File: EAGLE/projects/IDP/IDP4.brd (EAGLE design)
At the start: 100 x 80 mm, 14 parts, among them IC1 LM348P, M1 IDP_PROTOBOARD, U1 LM393P

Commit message: Added LED :+1:
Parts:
- added LED1, LED2, LED3: LED_23MM, IDP_library:LED3MM
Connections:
- new net ERROR_SENSOR_MALF: LED2.A, M1.D2
- new net ERROR_SIGNAL: LED3.A, M1.D0
- net GND: now also LED2.K, LED3.K
- net PHOTO_ON: now also LED1.A, LED1.K
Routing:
- net ERROR_SIGNAL: track 0.00 -> 20.3 mm, vias 0 -> 2
- net ERROR_SENSOR_MALF: track 0.00 -> 12.7 mm, vias 0 -> 2
- net GND: track 76.4 -> 86.5 mm
- net PHOTO_ON: track 45.6 -> 43.0 mm
- net +5V: track 53.3 -> 52.2 mm
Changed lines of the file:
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@@
 <attribute name="MF" value="MOLEX" x="60.96" y="55.88" size="1.778" layer="27" rot="R180" display="off"/>
 <attribute name="MPN" value="" x="60.96" y="55.88" size="1.778" layer="27" rot="R180" display="off"/>
-<attribute name="NAME" x="58.4469" y="51.5351" size="1.016" layer="25" ratio="10"/>
+<attribute name="NAME" x="54.6369" y="52.8051" size="1.016" layer="25" ratio="10"/>
 <attribute name="OC_FARNELL" value="unknown" x="60.96" y="55.88" size="1.778" layer="27" rot="R180" display="off"/>
 <attribute name="OC_NEWARK" value="unknown" x="60.96" y="55.88" size="1.778" layer="27" rot="R180" display="off"/>
 <attribute name="POPULARITY" value="0" x="60.96" y="55.88" size="1.778" layer="27" rot="R180" display="off"/>
-<attribute name="VALUE" x="71.0931" y="50.3189" size="0.8128" layer="27" ratio="10" rot="R180"/>
+<attribute name="VALUE" x="66.0131" y="51.5889" size="0.8128" layer="27" ratio="10" rot="R180"/>
 </element>
 <element name="SERVO" library="IDP_library" package="7395-03" package3d_urn="urn:adsk.eagle:package:8078646/1" value="Rapid 22-1010 /  22-0910" x="52.07" y="55.88" smashed="yes" rot="R180">
@@
 <attribute name="SPICEPREFIX" value="R" x="34.29" y="46.99" size="1.778" layer="27" rot="R270" display="off"/>
 <attribute name="VALUE" x="31.9786" y="49.1236" size="1.27" layer="27" ratio="10" rot="R270"/>
+</element>
+<element name="LED1" library="IDP_library" package="LED3MM" package3d_urn="urn:adsk.eagle:package:15797/1" value="LED_23MM" x="72.39" y="52.07" smashed="yes" rot="R90">
+<attribute name="NAME" x="75.819" y="50.165" size="1.27" layer="25" ratio="10" rot="R90"/>
+<attribute name="POPULARITY" value="97" x="72.39" y="52.07" size="1.778" layer="27" rot="R90" display="off"/>
+</element>
+<element name="LED2" library="IDP_library" package="LED3MM" package3d_urn="urn:adsk.eagle:package:15797/1" value="LED_23MM" x="67.31" y="49.53" smashed="yes" rot="R270">
+<attribute name="NAME" x="60.325" y="47.371" size="1.27" layer="25" ratio="10"/>
+<attribute name="POPULARITY" value="97" x="67.31" y="49.53" size="1.778" layer="27" rot="R270" display="off"/>
+</element>
+<element name="LED3" library="IDP_library" package="LED3MM" package3d_urn="urn:adsk.eagle:package:15797/1" value="LED_23MM" x="69.85" y="44.45" smashed="yes" rot="R270">
+<attribute name="NAME" x="71.755" y="42.291" size="1.27" layer="25" ratio="10"/>
+<attribute name="POPULARITY" value="97" x="69.85" y="44.45" size="1.778" layer="27" rot="R270" display="off"/>
 </element>
 </elements>
@@
 <wire x1="16.51" y1="48.26" x2="16.51" y2="40.64" width="0.1524" layer="1"/>
 <via x="16.51" y="40.64" extent="1-16" drill="0.35"/>
+<contactref element="LED2" pad="K"/>
+<contactref element="LED3" pad="K"/>
+<wire x1="67.31" y1="48.26" x2="67.31" y2="40.64" width="0.1524" layer="16"/>
+<wire x1="69.85" y1="43.18" x2="69.85" y2="40.64" width="0.1524" layer="16"/>
 </signal>
 <signal name="+3V3">
@@
 <wire x1="54.61" y1="55.88" x2="54.61" y2="58.42" width="0.1524" layer="16"/>
 <wire x1="64.77" y1="55.88" x2="64.77" y2="58.42" width="0.1524" layer="16"/>
-<wire x1="72.39" y1="38.1" x2="69.85" y2="35.56" width="0.1524" layer="16"/>
-<wire x1="69.85" y1="35.56" x2="69.85" y2="33.02" width="0.1524" layer="16"/>
 <wire x1="62.23" y1="22.86" x2="62.23" y2="30.48" width="0.1524" layer="16"/>
 <wire x1="62.23" y1="38.1" x2="62.23" y2="30.48" width="0.1524" layer="16"/>
+<wire x1="69.85" y1="38.1" x2="69.85" y2="35.56" width="0.1524" layer="16"/>
+<wire x1="69.85" y1="35.56" x2="69.85" y2="33.02" width="0.1524" layer="16"/>
+<wire x1="69.85" y1="35.56" x2="69.85" y2="35.56" width="0.1524" layer="16"/>
 </signal>
 <signal name="MOTOR_CHANNEL_A_DIRECTION">
@@
 <via x="72.39" y="46.99" extent="1-16" drill="0.35"/>
 <wire x1="46.99" y1="46.99" x2="72.39" y2="46.99" width="0.1524" layer="1"/>
-<wire x1="72.39" y1="55.88" x2="72.39" y2="46.99" width="0.1524" layer="16"/>
+<contactref element="LED1" pad="A"/>
+<contactref element="LED1" pad="K"/>
+<wire x1="72.39" y1="55.88" x2="72.39" y2="53.34" width="0.1524" layer="16"/>
+<wire x1="72.39" y1="50.8" x2="72.39" y2="46.99" width="0.1524" layer="16"/>
+<wire x1="72.39" y1="50.8" x2="72.39" y2="53.34" width="0" layer="19" extent="1-1"/>
 </signal>
 <signal name="N$1">
@@
 <wire x1="31.75" y1="55.88" x2="31.75" y2="43.18" width="0.1524" layer="16"/>
 </signal>
+<signal name="N$6">
+<via x="69.85" y="55.88" extent="1-16" drill="0.35"/>
+</signal>
+<signal name="ERROR_SIGNAL">
+<contactref element="M1" pad="D0"/>
+<contactref element="LED3" pad="A"/>
+<via x="74.93" y="60.96" extent="1-16" drill="0.35"/>
+<via x="74.93" y="45.72" extent="1-16" drill="0.35"/>
+<wire x1="74.93" y1="60.96" x2="74.93" y2="45.72" width="0.1524" layer="1"/>
+<wire x1="69.85" y1="45.72" x2="74.93" y2="45.72" width="0.1524" layer="1"/>
+</signal>
+<signal name="ERROR_SENSOR_MALF">
+<contactref element="M1" pad="D2"/>
+<contactref element="LED2" pad="A"/>
+<via x="67.31" y="55.88" extent="1-16" drill="0.35"/>
+<wire x1="67.31" y1="50.8" x2="67.31" y2="55.88" width="0.1524" layer="16"/>
+<via x="69.85" y="60.96" extent="1-16" drill="0.35"/>
+<wire x1="69.85" y1="60.96" x2="68.58" y2="60.96" width="0.1524" layer="1"/>
+<wire x1="68.58" y1="60.96" x2="68.58" y2="55.88" width="0.1524" layer="1"/>
+<wire x1="68.58" y1="55.88" x2="67.31" y2="55.88" width="0.1524" layer="1"/>
+</signal>
 </signals>

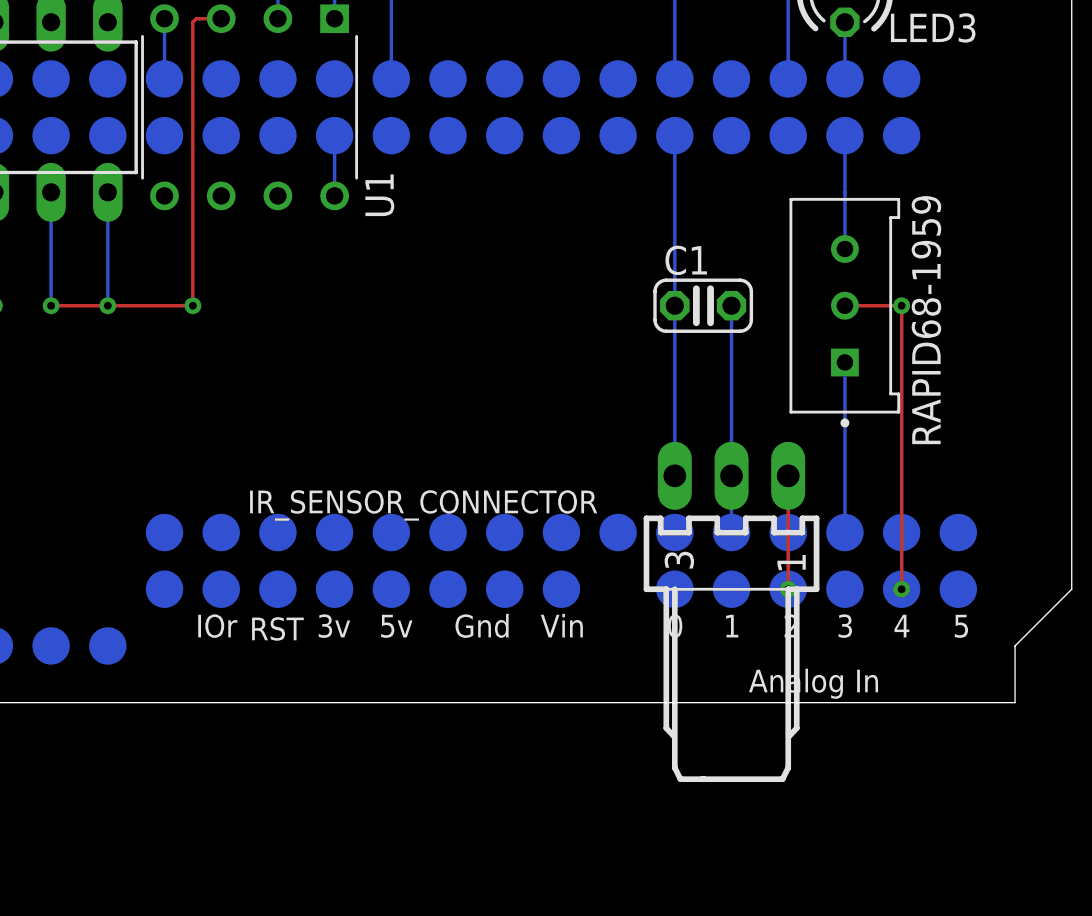
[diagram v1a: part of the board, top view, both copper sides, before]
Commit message: Added low pass filter
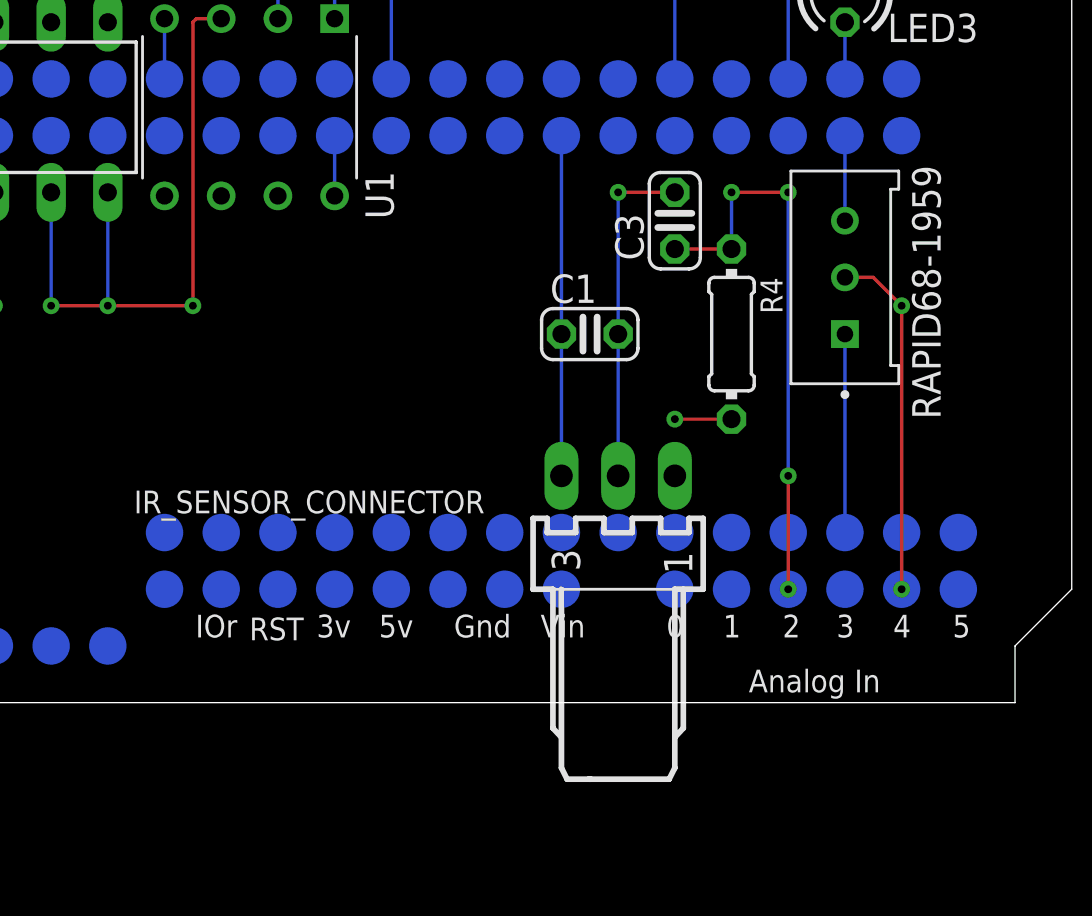
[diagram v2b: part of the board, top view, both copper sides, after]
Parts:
- added C3: 100n, IDP_library:C025-024X044
- added R4: 10k, IDP_library:0204/7
- moved C1 5.24 mm to (57.1, 29.2)
- moved IR_SENSOR_CONNECTOR 5.08 mm to (59.7, 22.9)
- moved RAPID68-1959 1.27 mm to (69.8, 31.8)
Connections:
- new net N$5: IR_SENSOR_CONNECTOR.1, R4.2
- net GND: now also C3.2
- net IR_SENSOR_VALUES: now also C3.1, R4.1; no longer IR_SENSOR_CONNECTOR.1
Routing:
- net IR_SENSOR_VALUES: track 5.08 -> 25.4 mm, vias 1 -> 4
- net GND: track 86.5 -> 92.9 mm, vias 3 -> 4
- net N$5: track 0.00 -> 2.54 mm, vias 0 -> 1
- net +5V: track 52.2 -> 51.0 mm
- net SERVO_ANALOG: track 15.2 -> 15.8 mm
